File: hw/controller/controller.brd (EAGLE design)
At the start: 46 x 53 mm, 127 parts, among them J1 XT30XT30PW_MALE, J2 XT30XT30PW_MALE, M1 MOUNT, M2 MOUNT, M3 MOUNT, M4 MOUNT, Q1 TPH1R204PLSOP_ADVANCE_8, Q2 TPH1R204PLSOP_ADVANCE_8, Q3 TPH1R204PLSOP_ADVANCE_8, Q4 TPH1R204PLSOP_ADVANCE_8, Q5 TPH1R204PLSOP_ADVANCE_8, Q6 TPH1R204PLSOP_ADVANCE_8, U1 STM32G474CEU6, U2 TCAN334GSOT23, U3 AS5147, U4 MAX15062AATA+T, U5 DRV8353S

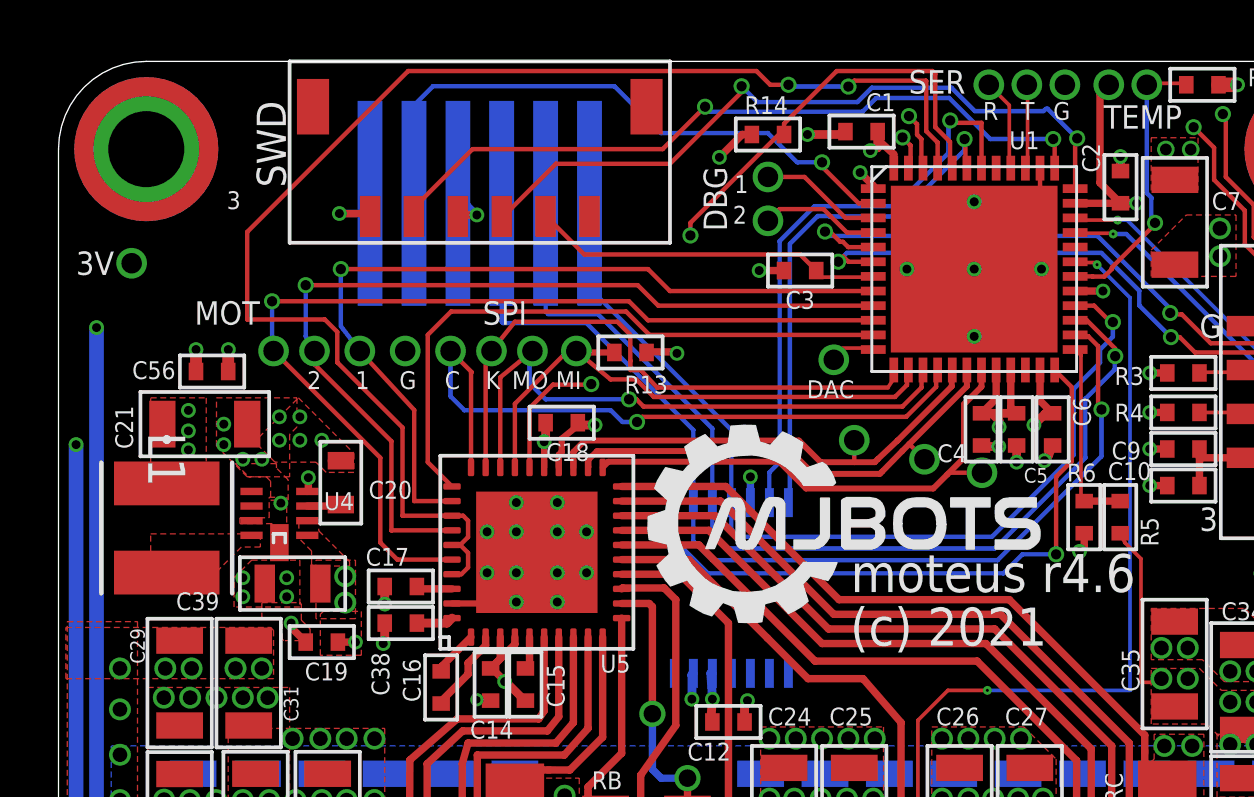
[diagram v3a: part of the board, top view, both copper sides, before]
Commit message: Tweak silk positions
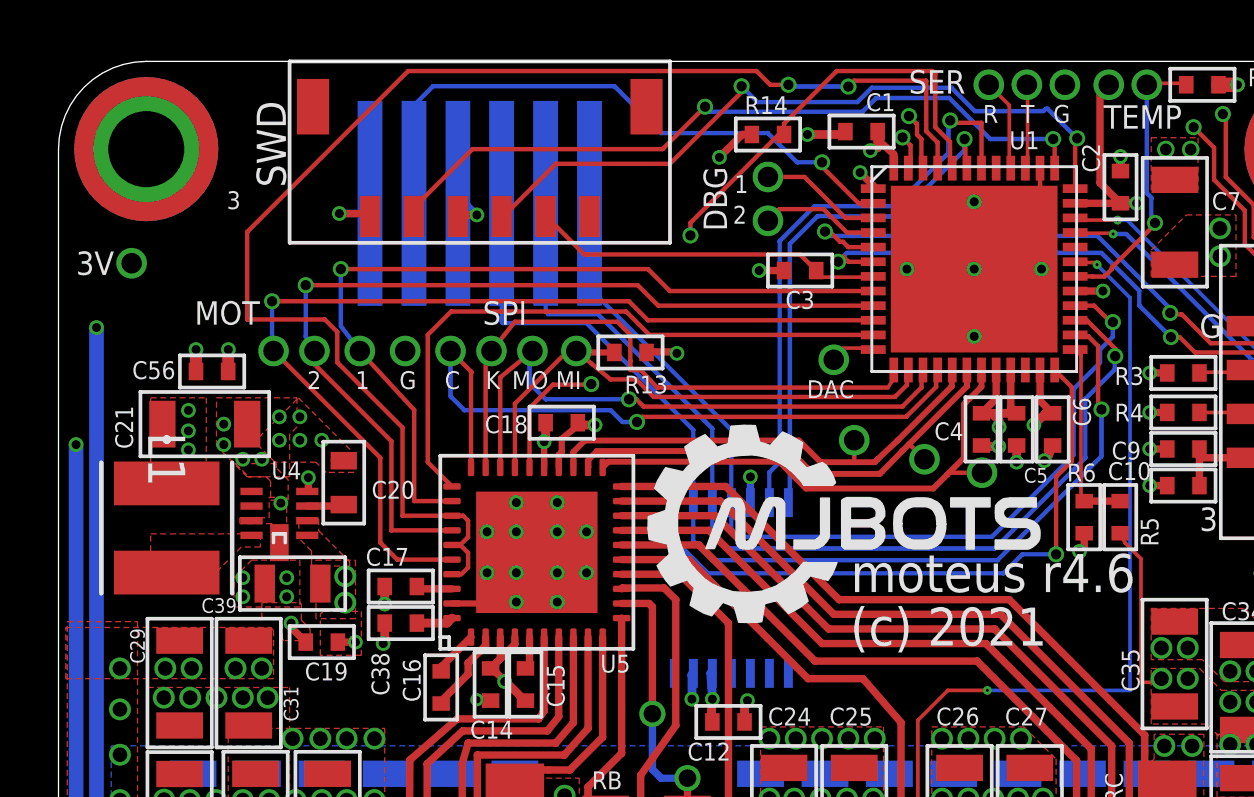
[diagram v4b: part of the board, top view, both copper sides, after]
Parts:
- moved C20 0.10 mm to (-13.2, -4.40)
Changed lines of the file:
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@@
 <text x="8" y="9.7" size="0.8" layer="21" rot="R180">SER</text>
 <text x="-0.95" y="6.4" size="0.8" layer="21" rot="R270">DBG</text>
-<text x="9.9" y="8" size="0.6096" layer="21" font="vector">T</text>
-<text x="8.6" y="8" size="0.6096" layer="21" font="vector">R</text>
+<text x="9.9" y="7.9" size="0.6096" layer="21" font="vector">T</text>
+<text x="8.6" y="7.9" size="0.6096" layer="21" font="vector">R</text>
 <text x="0.05" y="4.45" size="0.6096" layer="21" font="vector">2</text>
 <text x="0.1" y="5.5" size="0.6096" layer="21" font="vector">1</text>
@@
 <text x="-17.25" y="4.95" size="0.6096" layer="21" font="vector">3</text>
 <text x="-18.35" y="1" size="0.8" layer="21">MOT</text>
-<text x="11" y="8" size="0.6096" layer="21" font="vector">G</text>
+<text x="11" y="7.9" size="0.6096" layer="21" font="vector">G</text>
 <text x="-21.1" y="3.5" size="0.8" layer="21" rot="R180">3V</text>
 <text x="-11.35" y="-1.2" size="0.6096" layer="21" font="vector">G</text>
@@
 <attribute name="MF" value="" x="-5.8" y="-2.35" size="1.778" layer="27" display="off"/>
 <attribute name="MPN" value="MF-CAP-0402-0.1uF" x="-5.8" y="-2.35" size="1.778" layer="27" display="off"/>
-<attribute name="NAME" x="-4.85" y="-3.05" size="0.6096" layer="25" font="vector" ratio="10" rot="R180"/>
+<attribute name="NAME" x="-6.95" y="-2.1" size="0.6096" layer="25" font="vector" ratio="10" rot="R180"/>
 <attribute name="POPULATE" value="1" x="-5.8" y="-2.35" size="1.778" layer="27" display="off"/>
 <attribute name="TOLERANCE" value="" x="-5.8" y="-2.35" size="1.778" layer="27" display="off"/>
@@
 <attribute name="MF" value="" x="8.55" y="-2.58" size="1.778" layer="27" rot="R270" display="off"/>
 <attribute name="MPN" value="MF-CAP-0402-1uF" x="8.55" y="-2.58" size="1.778" layer="27" rot="R270" display="off"/>
-<attribute name="NAME" x="8.04" y="-3.09" size="0.6096" layer="25" font="vector" ratio="10" rot="R180"/>
+<attribute name="NAME" x="7.94" y="-2.34" size="0.6096" layer="25" font="vector" ratio="10" rot="R180"/>
 <attribute name="POPULATE" value="1" x="8.55" y="-2.58" size="1.778" layer="27" rot="R270" display="off"/>
 <attribute name="TOLERANCE" value="" x="8.55" y="-2.58" size="1.778" layer="27" rot="R270" display="off"/>
@@
 <attribute name="MANUFACTURER_PART_NUMBER" value="MAX15062AATA+T" x="-15.45" y="-16" size="1.778" layer="27" rot="R180" display="off"/>
 <attribute name="MPN" value="MAX15062AATA+T" x="-15.45" y="-16" size="1.778" layer="27" rot="R180" display="off"/>
-<attribute name="NAME" x="-13.9266" y="-5.335" size="0.6096" layer="25" ratio="10" rot="SR0"/>
+<attribute name="NAME" x="-15.7266" y="-4.285" size="0.6096" layer="25" ratio="10" rot="SR0"/>
 <attribute name="POPULATE" value="1" x="-15.45" y="-16" size="1.778" layer="27" rot="R180" display="off"/>
 <attribute name="REVISION" value="1" x="-15.45" y="-16" size="1.778" layer="27" rot="R180" display="off"/>
@@
 <attribute name="VENDOR" value="Maxim Integrated Products" x="-15.45" y="-16" size="1.778" layer="27" rot="R180" display="off"/>
 </element>
-<element name="C20" library="mfpassives" package="C0603" value="1uF" x="-13.35" y="-4.4" smashed="yes" rot="R90">
-<attribute name="DIELECTRIC" value="" x="-15" y="-4.4" size="1.778" layer="27" rot="R90" display="off"/>
-<attribute name="HOUSEPART" value="1" x="-15" y="-4.4" size="1.778" layer="27" rot="R90" display="off"/>
-<attribute name="MPN" value="MF-CAP-0603-1uF" x="-15" y="-4.4" size="1.778" layer="27" rot="R90" display="off"/>
-<attribute name="NAME" x="-12.4" y="-4.95" size="0.6096" layer="25" font="vector" ratio="10"/>
-<attribute name="POPULATE" value="1" x="-15" y="-4.4" size="1.778" layer="27" rot="R90" display="off"/>
-<attribute name="TOLERANCE" value="" x="-15" y="-4.4" size="1.778" layer="27" rot="R90" display="off"/>
-<attribute name="URL" value="" x="-15" y="-4.4" size="1.778" layer="27" rot="R90" display="off"/>
-<attribute name="VOLTAGE" value="" x="-15" y="-4.4" size="1.778" layer="27" rot="R90" display="off"/>
+<element name="C20" library="mfpassives" package="C0603" value="1uF" x="-13.25" y="-4.4" smashed="yes" rot="R90">
+<attribute name="DIELECTRIC" value="" x="-14.9" y="-4.4" size="1.778" layer="27" rot="R90" display="off"/>
+<attribute name="HOUSEPART" value="1" x="-14.9" y="-4.4" size="1.778" layer="27" rot="R90" display="off"/>
+<attribute name="MPN" value="MF-CAP-0603-1uF" x="-14.9" y="-4.4" size="1.778" layer="27" rot="R90" display="off"/>
+<attribute name="NAME" x="-12.3" y="-4.95" size="0.6096" layer="25" font="vector" ratio="10"/>
+<attribute name="POPULATE" value="1" x="-14.9" y="-4.4" size="1.778" layer="27" rot="R90" display="off"/>
+<attribute name="TOLERANCE" value="" x="-14.9" y="-4.4" size="1.778" layer="27" rot="R90" display="off"/>
+<attribute name="URL" value="" x="-14.9" y="-4.4" size="1.778" layer="27" rot="R90" display="off"/>
+<attribute name="VOLTAGE" value="" x="-14.9" y="-4.4" size="1.778" layer="27" rot="R90" display="off"/>
 </element>
 <element name="C21" library="mfpassives" package="C1206" value="10uF" x="-18" y="-2.4" smashed="yes">
@@
 <attribute name="MF" value="MURATA" x="-10" y="4.95" size="1.778" layer="27" rot="R180" display="off"/>
 <attribute name="MPN" value="GCM21BC72A105KE36L" x="-10" y="4.95" size="1.778" layer="27" rot="R180" display="off"/>
-<attribute name="NAME" x="-17.5" y="-8.15" size="0.6096" layer="25" font="vector" ratio="10" rot="R180"/>
+<attribute name="NAME" x="-16.9" y="-8.35" size="0.5" layer="25" font="vector" ratio="10" rot="R180"/>
 <attribute name="POPULATE" value="1" x="-10" y="4.95" size="1.778" layer="27" rot="R180" display="off"/>
 <attribute name="TOLERANCE" value="" x="-10" y="4.95" size="1.778" layer="27" rot="R180" display="off"/>
@@
 <wire x1="11.75" y1="2.15" x2="12.7" y2="2.15" width="0.254" layer="1"/>
 <via x="-15.4" y="-5.1" extent="1-16" drill="0.3048"/>
-<wire x1="-13.35" y1="-3.65" x2="-13.65" y2="-3.65" width="0.3048" layer="1"/>
+<wire x1="-13.25" y1="-3.65" x2="-13.55" y2="-3.65" width="0.3048" layer="1"/>
 <wire x1="-9.35" y1="5.15" x2="-9.1" y2="5.15" width="0.254" layer="16"/>
 <wire x1="-9.1" y1="5.15" x2="-8.7" y2="4.75" width="0.254" layer="16"/>
@@
 <contactref element="U4" pad="3"/>
 <contactref element="C20" pad="P$1"/>
-<wire x1="-13.35" y1="-5.15" x2="-13.4" y2="-5.2" width="0.2032" layer="1"/>
-<wire x1="-13.4" y1="-5.2" x2="-14.4975" y2="-5.2" width="0.254" layer="1"/>
+<wire x1="-13.25" y1="-5.15" x2="-13.3" y2="-5.2" width="0.2032" layer="1"/>
+<wire x1="-13.3" y1="-5.2" x2="-14.4975" y2="-5.2" width="0.254" layer="1"/>
 </signal>
 <signal name="VSW">

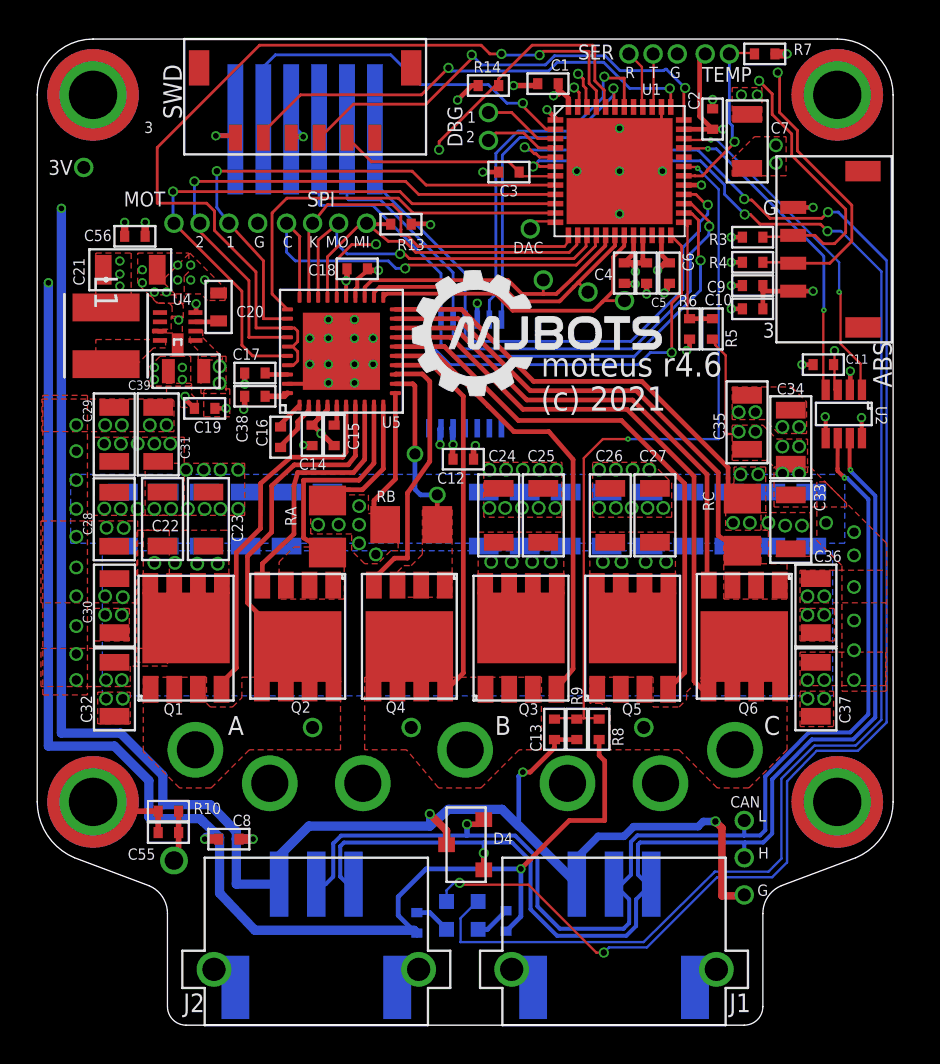
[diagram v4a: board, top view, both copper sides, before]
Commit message: r4.6: Add room for a common mode choke on the CAN-FD lines
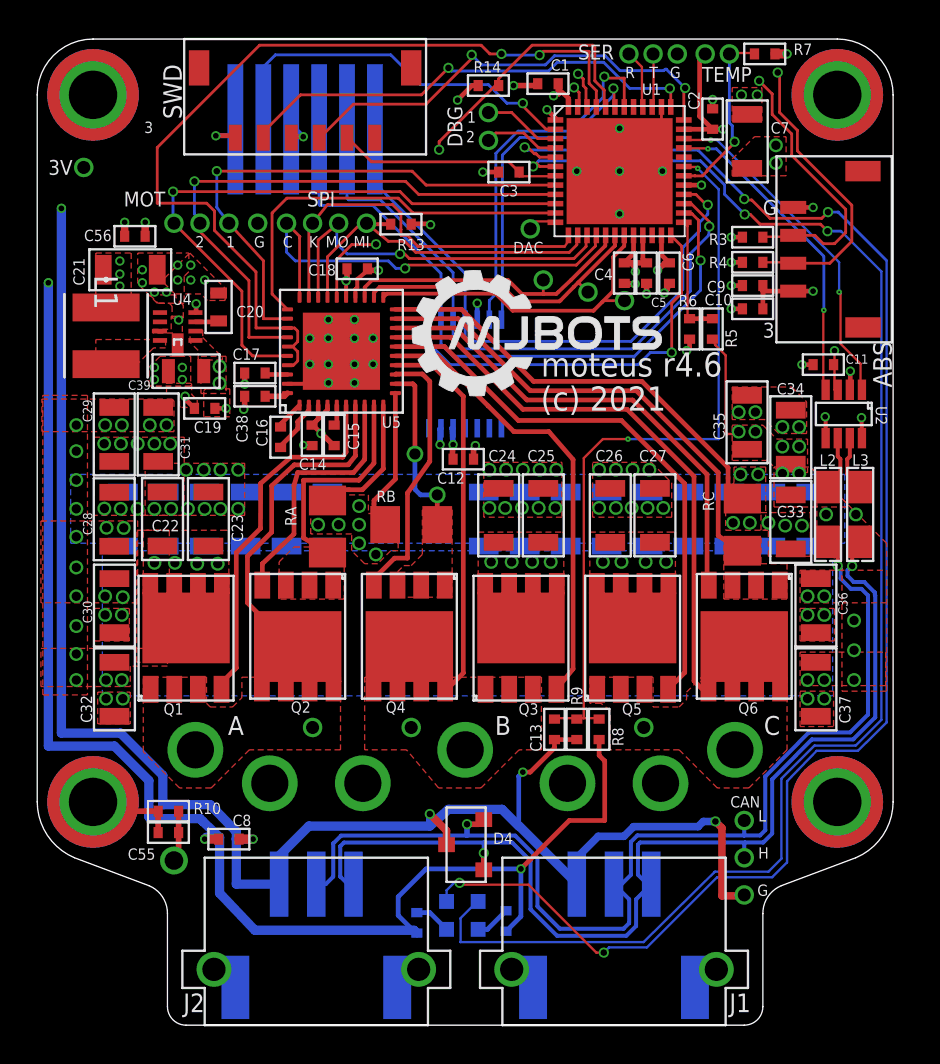
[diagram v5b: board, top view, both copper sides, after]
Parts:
- added L2, L3: HALF_CHOKE, controller:1812_COMMON_HALF
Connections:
- new net CAN2_N: L2.P$2, U2.6
- new net CAN2_P: L3.P$2, U2.7
- net CAN_N: now also L2.P$1; no longer U2.6
- net CAN_P: now also L3.P$1; no longer U2.7
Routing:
- net CAN_N: track 63.3 -> 58.2 mm
- net CAN_P: track 62.6 -> 57.7 mm
- net CAN2_P: track 0.00 -> 2.98 mm
- net CAN2_N: track 0.00 -> 2.96 mm
- net V+: vias 53 -> 51

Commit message: r4.6: More trace and poly tweaks
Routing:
- net GND: track 115.0 -> 116.1 mm
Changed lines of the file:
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@@
 <via x="-19.275" y="-16.265" extent="1-16" drill="0.5"/>
 <via x="-19.35" y="-19.95" extent="1-16" drill="0.5"/>
-<via x="-18.4" y="-20" extent="1-16" drill="0.5"/>
+<via x="-18.4" y="-19.95" extent="1-16" drill="0.5"/>
 <via x="-16.95" y="-10.75" extent="1-16" drill="0.5"/>
 <via x="-16.05" y="-10.75" extent="1-16" drill="0.5"/>
@@
 </polygon>
 <polygon width="0.127" layer="1" isolate="0.5" orphans="yes" thermals="no">
-<vertex x="18.9" y="-13.8"/>
+<vertex x="18.9" y="-16.15"/>
 <vertex x="18.9" y="-16.95"/>
 <vertex x="20.25" y="-18.3"/>
 <vertex x="20.25" y="-25.05"/>
-<vertex x="22.65" y="-25.05"/>
-<vertex x="22.65" y="-17.1"/>
-<vertex x="19.35" y="-13.8"/>
+<vertex x="22.75" y="-25.05"/>
+<vertex x="22.75" y="-16.15"/>
 </polygon>
 <via x="-20.9" y="-10.75" extent="1-16" drill="0.5"/>
@@
 <vertex x="-4.4" y="-4.25"/>
 <vertex x="-4.4" y="-12.8"/>
-<vertex x="11.5" y="-12.8"/>
-<vertex x="14.6" y="-9.7"/>
-<vertex x="18.8" y="-9.7"/>
-<vertex x="18.8" y="-16.1"/>
-<vertex x="22.4" y="-16.1"/>
-<vertex x="22.4" y="-42.5"/>
+<vertex x="10" y="-12.8"/>
+<vertex x="13.1" y="-9.7"/>
+<vertex x="19.65" y="-9.7"/>
+<vertex x="19.65" y="-12.15"/>
+<vertex x="22.45" y="-12.15"/>
+<vertex x="22.45" y="-42.5"/>
 </polygon>
 <contactref element="C33" pad="P$2"/>
@@
 <vertex x="-3.75" y="-3.6"/>
 <vertex x="-3.75" y="-12.05"/>
-<vertex x="11.259284375" y="-12.05"/>
-<vertex x="14.30214375" y="-9.05"/>
-<vertex x="19.25" y="-9.05"/>
-<vertex x="19.25" y="-16"/>
-<vertex x="22.4" y="-16"/>
+<vertex x="9.41" y="-12.05"/>
+<vertex x="12.452859375" y="-9.05"/>
+<vertex x="20.2" y="-9.05"/>
+<vertex x="20.2" y="-11.35"/>
+<vertex x="22.4" y="-11.35"/>
 <vertex x="22.4" y="9.5"/>
 <vertex x="-22.5" y="9.5"/>
@@
 <via x="20.7" y="-7.85" extent="1-16" drill="0.3048"/>
 <via x="21.3" y="-10.35" extent="1-16" drill="0.3048"/>
-<via x="19.35" y="-10.3" extent="1-16" drill="0.3048"/>
-<wire x1="19.375" y1="-11.45" x2="19.375" y2="-10.308475" width="0.2159" layer="1"/>
-<wire x1="19.375" y1="-10.308475" x2="19.35" y2="-10.3" width="0.2159" layer="1"/>
+<via x="20.55" y="-10.35" extent="1-16" drill="0.3048"/>
+<wire x1="19.375" y1="-11.45" x2="19.37726875" y2="-10.3575875" width="0.2159" layer="1"/>
+<wire x1="19.37726875" y1="-10.3575875" x2="20.55" y2="-10.35" width="0.2159" layer="1"/>
 <wire x1="21.325" y1="-11.45" x2="21.325" y2="-11.35" width="0.2159" layer="1"/>
 <wire x1="21.325" y1="-11.35" x2="21.3" y2="-10.35" width="0.2159" layer="1"/>
@@
 <wire x1="-6.71355" y1="-35.015" x2="-6.30855" y2="-35.42" width="0.2159" layer="16"/>
 <wire x1="-6.30855" y1="-35.42" x2="-6" y2="-35.42" width="0.2159" layer="16"/>
-<wire x1="22.04145" y1="-26.45601875" x2="22.04145" y2="-19.900903125" width="0.2159" layer="16"/>
 <wire x1="22.04145" y1="-26.45601875" x2="20.85601875" y2="-27.64145" width="0.2159" layer="16"/>
 <wire x1="20.85601875" y1="-27.64145" x2="18.635096875" y2="-27.64145" width="0.2159" layer="16"/>
@@
 <wire x1="1.01125" y1="-33.18645" x2="2.52898125" y2="-33.18645" width="0.2159" layer="16"/>
 <contactref element="L3" pad="P$1"/>
-<wire x1="22.04145" y1="-19.900903125" x2="22.0183" y2="-19.877753125" width="0.2159" layer="16"/>
-<wire x1="22.0183" y1="-19.877753125" x2="22.0183" y2="-19.74744375" width="0.2159" layer="16"/>
-<wire x1="22.0183" y1="-19.74744375" x2="21.45255625" y2="-19.1817" width="0.2159" layer="16"/>
+<wire x1="22.04145" y1="-26.45601875" x2="22.04145" y2="-19.77059375" width="0.2159" layer="16"/>
+<wire x1="22.04145" y1="-19.77059375" x2="21.45255625" y2="-19.1817" width="0.2159" layer="16"/>
 <wire x1="20.55" y1="-18.85" x2="20.55" y2="-18.55" width="0.2159" layer="16"/>
 <wire x1="20.8817" y1="-19.1817" x2="20.55" y2="-18.85" width="0.2159" layer="16"/>
 <wire x1="21.45255625" y1="-19.1817" x2="20.8817" y2="-19.1817" width="0.2159" layer="16"/>
 <wire x1="20.55" y1="-18.55" x2="20.776" y2="-18.324" width="0.2159" layer="16"/>
-<wire x1="20.776" y1="-18.324" x2="20.8" y2="-18.324" width="0.2159" layer="16"/>
-<via x="20.8" y="-18.324" extent="1-16" drill="0.35"/>
-<wire x1="20.8" y1="-18.324" x2="20.8" y2="-17.45" width="0.2159" layer="1"/>
+<wire x1="20.776" y1="-18.324" x2="20.8" y2="-18.31" width="0.2159" layer="16"/>
+<via x="20.8" y="-18.31" extent="1-16" drill="0.35"/>
+<wire x1="20.8" y1="-18.31" x2="20.8" y2="-17.45" width="0.2159" layer="1"/>
 <wire x1="20.8" y1="-17.45" x2="21.23" y2="-17.02" width="0.2159" layer="1"/>
 </signal>
@@
 <wire x1="20.7291375" y1="-19.55" x2="20.1817" y2="-19.0025625" width="0.2159" layer="16"/>
 <wire x1="21.3" y1="-19.55" x2="20.7291375" y2="-19.55" width="0.2159" layer="16"/>
-<wire x1="20.1817" y1="-18.475" x2="20.02366875" y2="-18.31696875" width="0.2159" layer="16"/>
-<via x="20.02366875" y="-18.31696875" extent="1-16" drill="0.35"/>
-<wire x1="20.02366875" y1="-18.31696875" x2="20.02366875" y2="-17.54366875" width="0.2159" layer="1"/>
+<wire x1="20.1817" y1="-18.475" x2="20.02366875" y2="-18.31" width="0.2159" layer="16"/>
+<via x="20.02366875" y="-18.31" extent="1-16" drill="0.35"/>
+<wire x1="20.02366875" y1="-18.31" x2="20.02366875" y2="-17.54366875" width="0.2159" layer="1"/>
 <wire x1="20.02366875" y1="-17.54366875" x2="19.5" y2="-17.02" width="0.2159" layer="1"/>
 <wire x1="20.1817" y1="-19.0025625" x2="20.1817" y2="-18.475" width="0.2159" layer="16"/>
